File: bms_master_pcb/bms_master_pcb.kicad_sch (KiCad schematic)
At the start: 0 parts

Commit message: changes made during ICD meeting.
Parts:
- added U1: STM32G474RETx, Package_QFP:LQFP-64_10x10mm_P0.5mm, symbol MCU_ST_STM32G4:STM32G474RETx
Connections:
- new net: U1.15 (VSS), U1.31 (VSS), U1.47 (VSS), U1.63 (VSS)
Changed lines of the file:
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@@
 	(generator_version "10.0")
 	(paper "A4")
+	(symbol
+		(lib_id "MCU_ST_STM32G4:STM32G474RETx")
+		(at 106.68 101.6 0)
+		(unit 1)
+		(body_style 1)
+		(exclude_from_sim no)
+		(in_bom yes)
+		(on_board yes)
+		(in_pos_files yes)
+		(dnp no)
+		(fields_autoplaced yes)
+		(property "Reference" "U1"
+			(at 111.3633 149.86 0)
+			(show_name no)
+			(do_not_autoplace no)
+			(effects
+				(font
+					(size 1.27 1.27)
+				)
+				(justify left)
+			)
+		)
+		(property "Value" "STM32G474RETx"
+			(at 111.3633 152.4 0)
+			(show_name no)
+			(do_not_autoplace no)
+			(effects
+				(font
+					(size 1.27 1.27)
+				)
+				(justify left)
+			)
+		)
+		(property "Footprint" "Package_QFP:LQFP-64_10x10mm_P0.5mm"
+			(at 91.44 147.32 0)
+			(hide yes)
+			(show_name no)
+			(do_not_autoplace no)
+			(effects
+				(font
+					(size 1.27 1.27)
+				)
+				(justify right)
+			)
+		)
+		(property "Datasheet" "https://www.st.com/resource/en/datasheet/stm32g474re.pdf"
+			(at 106.68 101.6 0)
+			(hide yes)
+			(show_name no)
+			(do_not_autoplace no)
+			(effects
+				(font
+					(size 1.27 1.27)
+				)
+			)
+		)
+		(property "Description" "STMicroelectronics Arm Cortex-M4 MCU, 512KB flash, 128KB RAM, 170 MHz, 1.71-3.6V, 52 GPIO, LQFP64"
+			(at 106.68 101.6 0)
+			(hide yes)
+			(show_name no)
+			(do_not_autoplace no)
+			(effects
+				(font
+					(size 1.27 1.27)
+				)
+			)
+		)
+		(pin "20"
+		)
+		(pin "18"
+		)
+		(pin "3"
+		)
+		(pin "1"
+		)
+		(pin "4"
+		)
+		(pin "5"
+		)
+		(pin "6"
+		)
+		(pin "14"
+		)
+		(pin "15"
+		)
+		(pin "19"
+		)
+		(pin "17"
+		)
+		(pin "2"
+		)
+		(pin "7"
+		)
+		(pin "8"
+		)
+		(pin "9"
+		)
+		(pin "10"
+		)
+		(pin "11"
+		)
+		(pin "12"
+		)
+		(pin "13"
+		)
+		(pin "16"
+		)
+		(pin "21"
+		)
+		(pin "47"
+		)
+		(pin "29"
+		)
+		(pin "30"
+		)
+		(pin "37"
+		)
+		(pin "31"
+		)
+		(pin "34"
+		)
+		(pin "41"
+		)
+		(pin "23"
+		)
+		(pin "28"
+		)
+		(pin "22"
+		)
+		(pin "36"
+		)
+		(pin "43"
+		)
+		(pin "40"
+		)
+		(pin "24"
+		)
+		(pin "45"
+		)
+		(pin "53"
+		)
+		(pin "51"
+		)
+		(pin "52"
+		)
+		(pin "25"
+		)
+		(pin "27"
+		)
+		(pin "33"
+		)
+		(pin "35"
+		)
+		(pin "26"
+		)
+		(pin "32"
+		)
+		(pin "38"
+		)
+		(pin "39"
+		)
+		(pin "42"
+		)
+		(pin "44"
+		)
+		(pin "46"
+		)
+		(pin "48"
+		)
+		(pin "49"
+		)
+		(pin "50"
+		)
+		(pin "54"
+		)
+		(pin "64"
+		)
+		(pin "63"
+		)
+		(pin "57"
+		)
+		(pin "58"
+		)
+		(pin "55"
+		)
+		(pin "59"
+		)
+		(pin "62"
+		)
+		(pin "56"
+		)
+		(pin "61"
+		)
+		(pin "60"
+		)
+		(instances
+			(project "bms_master_pcb"
+				(path "/58d62284-ebd1-49ab-8e0b-414456219053"
+					(reference "U1")
+					(unit 1)
+				)
+			)
+		)
+	)
 	(sheet_instances
 		(path "/"

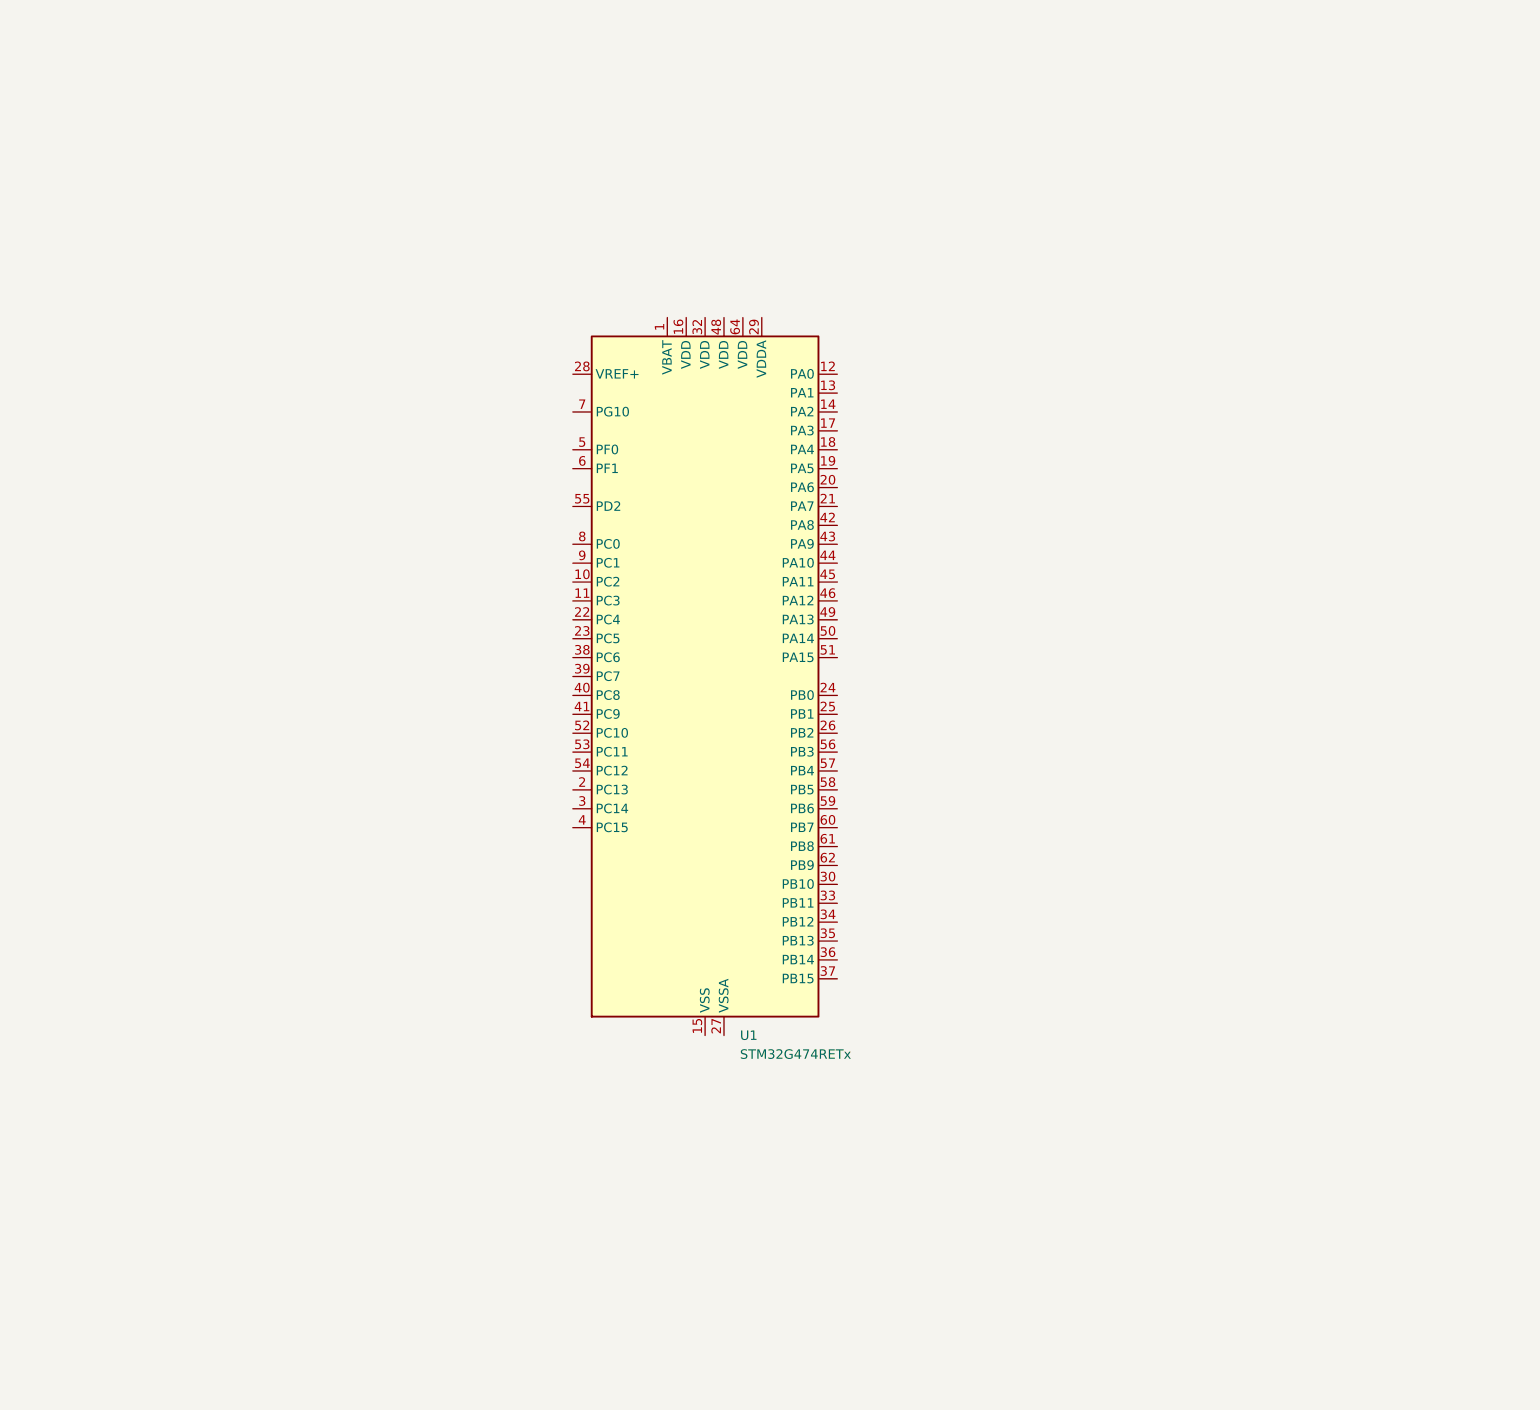
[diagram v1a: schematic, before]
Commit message: had to redo the master board after encountering an unfixable bug. bms_master_pcb2 is the one to keep working on.
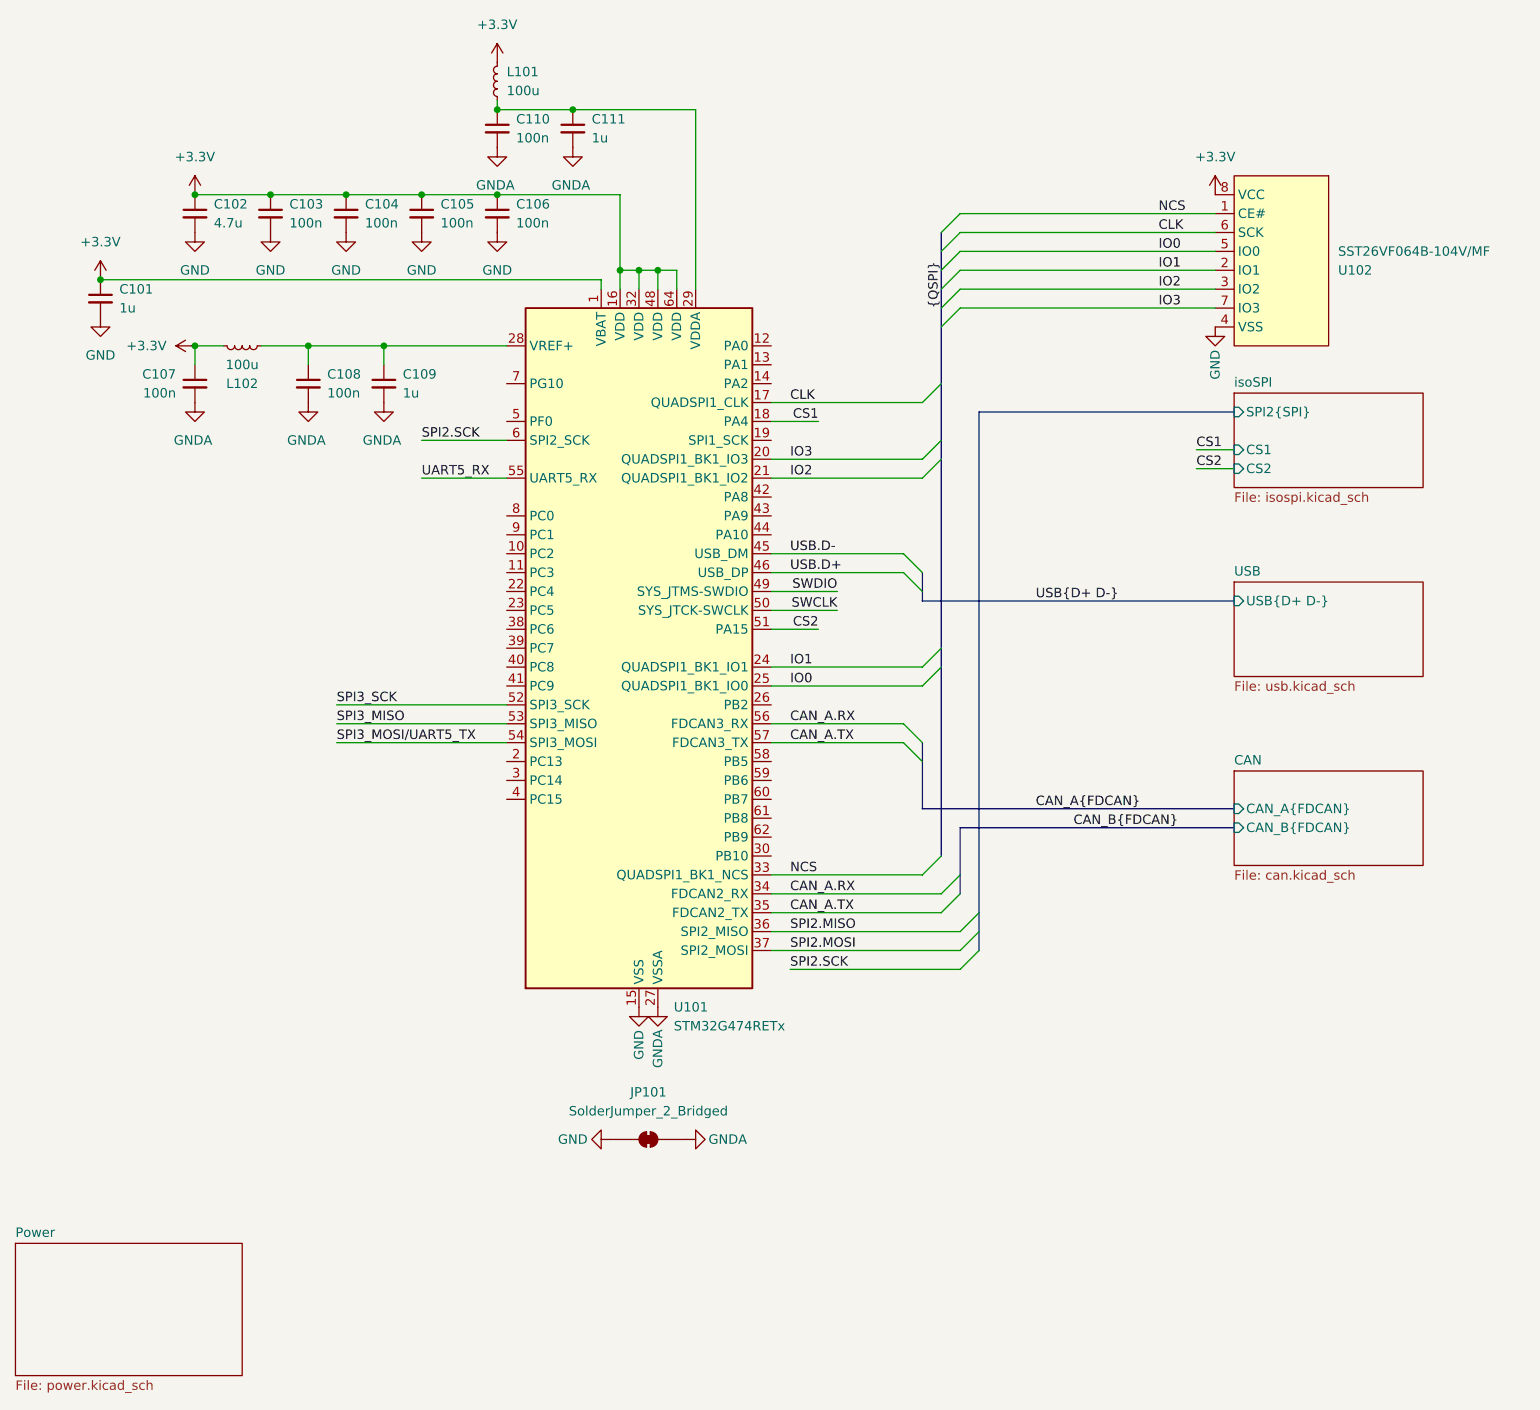
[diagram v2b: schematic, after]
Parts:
- added C101, C109, C111: 1u, symbol Device:C_Small
- added C102: 4.7u, symbol Device:C_Small
- added C103, C104, C105, C106, C107, C108, C110: 100n, symbol Device:C_Small
- added JP101: SolderJumper_2_Bridged, symbol Jumper:SolderJumper_2_Bridged
- added L101, L102: 100u, symbol Device:L_Small
- added U102: SST26VF064B-104V/MF, symbol work_symbols:SST26VF064B-104V/MF
- U101: renamed from U1; Ordering (none) -> https://www.mouser.com/ProductDetail/STMicroelectronics/STM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
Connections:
- net +3.3V: now reaches U101.1 (VBAT)
- net +3.3V: now also U101.16 (VDD), U101.32 (VDD), U101.48 (VDD), U101.64 (VDD), C101.1, C102.1, C103.1, C104.1, C105.1, C106.1, C107.1, L101.2, L102.2, U102.8 (VCC)
- net GND: now reaches U101.15 (VSS), U101.31 (VSS), U101.47 (VSS), U101.63 (VSS)
- net GND: now also C101.2, C102.2, C103.2, C104.2, C105.2, C106.2, JP101.1 (A), U102.4 (VSS)
- net CLK: now reaches U101.17 (PA3)
- net CLK: now also U102.6 (SCK)
- net CS1: now reaches U101.18 (PA4)
- net IO3: now reaches U101.20 (PA6)
- net IO3: now also U102.7 (HOLD)
- net IO2: now reaches U101.21 (PA7)
- net IO2: now also U102.3 (WP#)
- net IO1: now reaches U101.24 (PB0)
- net IO1: now also U102.2 (SO)
- net IO0: now reaches U101.25 (PB1)
- net IO0: now also U102.5 (SI)
- net GNDA: now reaches U101.27 (VSSA)
- net GNDA: now also C107.2, C108.2, C109.2, C110.2, C111.2, JP101.2 (B)
- net at U101.28 (VREF+): now also C108.1, C109.1, L102.1
- net at U101.29 (VDDA): now also C110.1, C111.1, L101.1
- net NCS: now reaches U101.33 (PB11)
- net NCS: now also U102.1 (CE#)
- net CAN_A.RX: now reaches U101.34 (PB12)
- net CAN_A.RX: now also U101.56 (PB3)
- net CAN_A.TX: now reaches U101.35 (PB13)
- net CAN_A.TX: now also U101.57 (PB4)
- net SPI2.MISO: now reaches U101.36 (PB14)
- net SPI2.MOSI: now reaches U101.37 (PB15)
- net USB.D-: now reaches U101.45 (PA11)
- net USB.D+: now reaches U101.46 (PA12)
- net SWDIO: now reaches U101.49 (PA13)
- net SWCLK: now reaches U101.50 (PA14)
- net CS2: now reaches U101.51 (PA15)
- net SPI3_SCK: now reaches U101.52 (PC10)
- net SPI3_MISO: now reaches U101.53 (PC11)
- net SPI3_MOSI/UART5_TX: now reaches U101.54 (PC12)
- net UART5_RX: now reaches U101.55 (PD2)
- net SPI2.SCK: now reaches U101.6 (PF1)
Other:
- added sheet CAN (can.kicad_sch)
- added sheet Power (power.kicad_sch)
- added sheet USB (usb.kicad_sch)
- added sheet isoSPI (isospi.kicad_sch)
- moved on the sheet: U101
